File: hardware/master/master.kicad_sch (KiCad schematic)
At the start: 0 parts

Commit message: Add master card master meter sheet
Stereo 12-segment peak meter after the master level: per-side
superdiode detectors with 1 ms attack and 1.5 s fall, one shared 1%
ladder (within 0.04 dB) and 24 LM339 comparators (decision 93).

Co-Authored-By: Claude Opus 5.5 <noreply@anthropic.com>
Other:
- added sheet Master meter (meter.kicad_sch)
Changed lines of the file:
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@@
 		)
 		(pin "MAIN_L_OUT" output
-			(at 190.5 96.52 0)
+			(at 190.5 96.52 0.0000)
 			(effects
 				(font
@@
 		)
 		(pin "MAIN_R_OUT" output
-			(at 190.5 99.06 0)
+			(at 190.5 99.06 0.0000)
 			(effects
 				(font
@@
 		)
 		(pin "RLY_N" output
-			(at 190.5 101.6 0)
+			(at 190.5 101.6 0.0000)
 			(effects
 				(font
@@
 				(path "/e58f7b8d-79d3-4449-9042-9214947ce872"
 					(page "9")
+				)
+			)
+		)
+	)
+	(sheet
+		(at 215.9 38.1)
+		(size 30.48 20.32)
+		(exclude_from_sim no)
+		(in_bom yes)
+		(on_board yes)
+		(dnp no)
+		(fields_autoplaced yes)
+		(stroke
+			(width 0.1524)
+			(type solid)
+		)
+		(fill
+			(color 0 0 0 0.0000)
+		)
+		(property "Sheetname" "Master meter"
+			(at 215.9 37.3884 0)
+			(effects
+				(font
+					(size 1.27 1.27)
+				)
+				(justify left bottom)
+			)
+		)
+		(property "Sheetfile" "meter.kicad_sch"
+			(at 215.9 59.0046 0)
+			(effects
+				(font
+					(size 1.27 1.27)
+				)
+				(justify left top)
+			)
+		)
+		(pin "MAIN_L_OUT" input
+			(at 215.9 40.64 180)
+			(effects
+				(font
+					(size 1.27 1.27)
+				)
+				(justify left)
+			)
+		)
+		(pin "MAIN_R_OUT" input
+			(at 215.9 43.18 180)
+			(effects
+				(font
+					(size 1.27 1.27)
+				)
+				(justify left)
+			)
+		)
+		(instances
+			(project "master"
+				(path "/e58f7b8d-79d3-4449-9042-9214947ce872"
+					(page "10")
 				)
 			)
@@
 	(wire (pts (xy 160.02 101.6) (xy 154.94 101.6)) (stroke (width 0) (type default)))
 	(label "MAIN_R_SUM" (at 154.94 101.6 180) (fields_autoplaced yes) (effects (font (size 1.27 1.27)) (justify right bottom)))
+	(wire (pts (xy 190.5 96.52) (xy 195.58 96.52)) (stroke (width 0) (type default)))
+	(label "MAIN_L_OUT" (at 195.58 96.52 0) (fields_autoplaced yes) (effects (font (size 1.27 1.27)) (justify left bottom)))
+	(wire (pts (xy 190.5 99.06) (xy 195.58 99.06)) (stroke (width 0) (type default)))
+	(label "MAIN_R_OUT" (at 195.58 99.06 0) (fields_autoplaced yes) (effects (font (size 1.27 1.27)) (justify left bottom)))
+	(wire (pts (xy 215.9 40.64) (xy 210.82 40.64)) (stroke (width 0) (type default)))
+	(label "MAIN_L_OUT" (at 210.82 40.64 180) (fields_autoplaced yes) (effects (font (size 1.27 1.27)) (justify right bottom)))
+	(wire (pts (xy 215.9 43.18) (xy 210.82 43.18)) (stroke (width 0) (type default)))
+	(label "MAIN_R_OUT" (at 210.82 43.18 180) (fields_autoplaced yes) (effects (font (size 1.27 1.27)) (justify right bottom)))
 	(sheet_instances
 		(path "/"

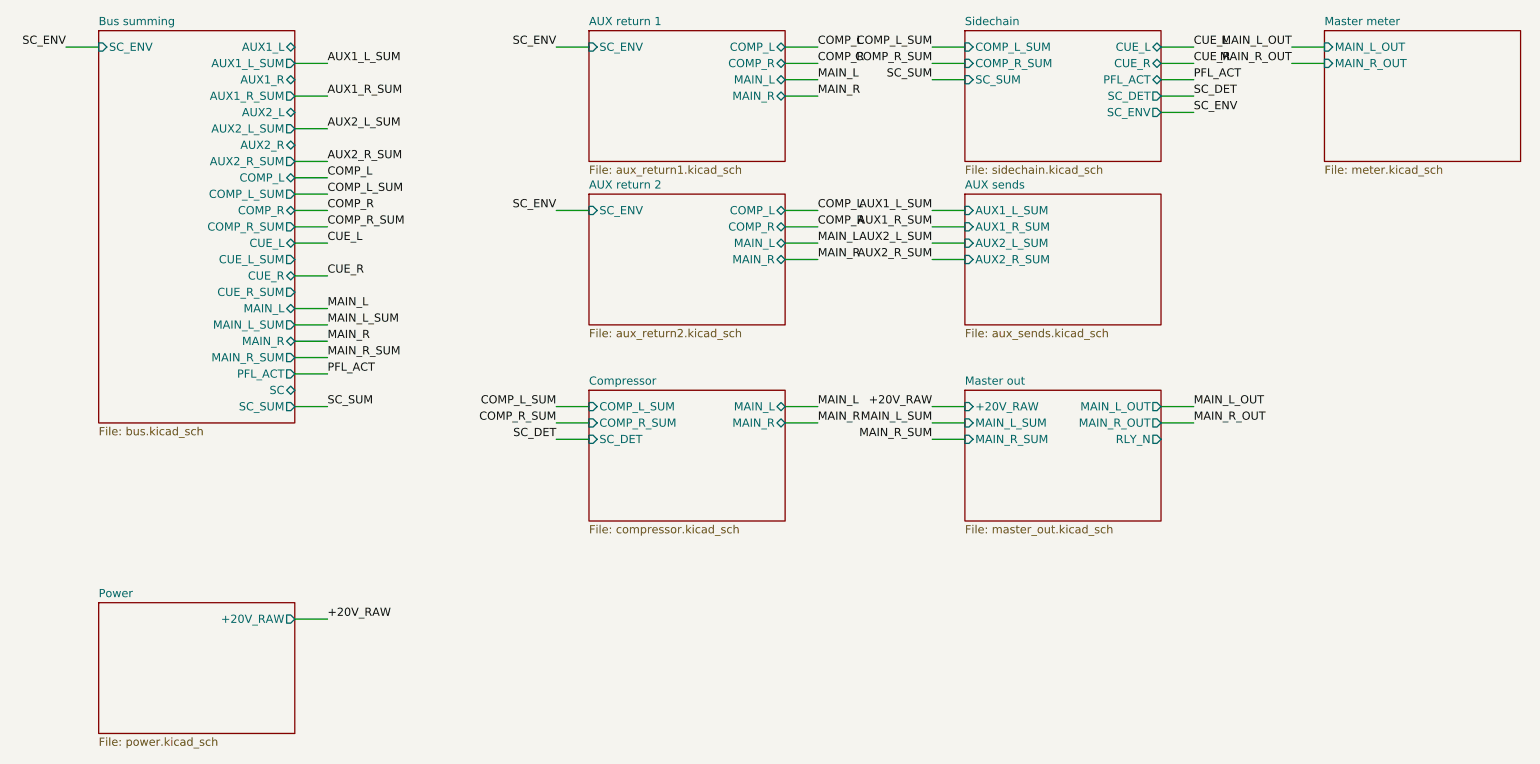
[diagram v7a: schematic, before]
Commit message: Add master card headphones sheet; master schematic complete
Main/cue source switch on PFL_ACT, dual volume pot, TPA6120A2 at
gain 2 with TI's resistor values, protection relay and PFL-active LED
(decision 94). Adds the TPA6120A2 symbol and no-connect flags for the
unused bus-node pins (root_nc.json). Master card ERC 0/0.

Co-Authored-By: Claude Opus 5.5 <noreply@anthropic.com>
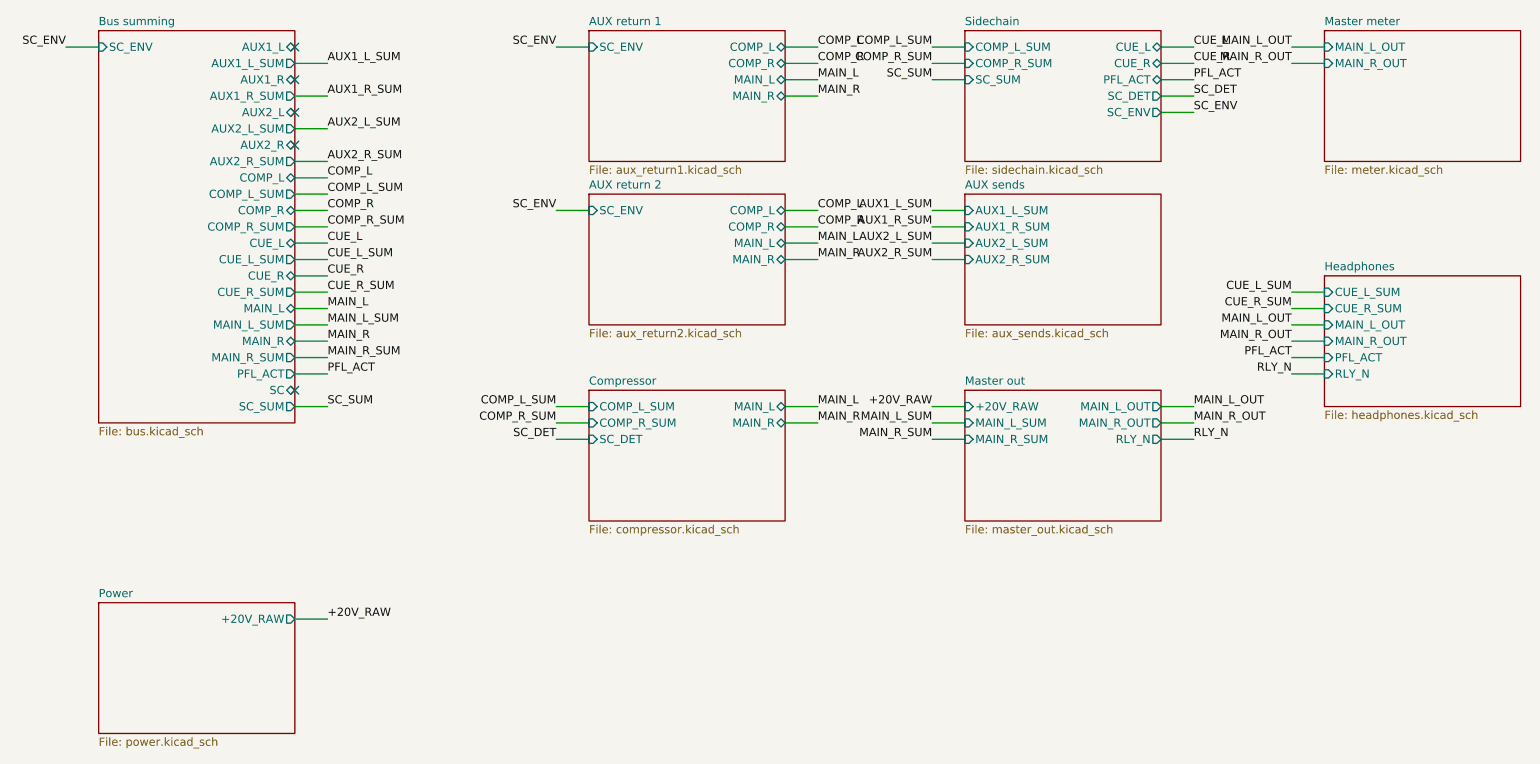
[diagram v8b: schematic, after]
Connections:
- no-connect marks 0 -> 5
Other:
- added sheet Headphones (headphones.kicad_sch)
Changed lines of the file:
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@@
+		)
+	)
+	(sheet
+		(at 215.9 76.2)
+		(size 30.48 20.32)
+		(exclude_from_sim no)
+		(in_bom yes)
+		(on_board yes)
+		(dnp no)
+		(fields_autoplaced yes)
+		(stroke
+			(width 0.1524)
+			(type solid)
+		)
+		(fill
+			(color 0 0 0 0.0000)
+		)
+		(property "Sheetname" "Headphones"
+			(at 215.9 75.4884 0)
+			(effects
+				(font
+					(size 1.27 1.27)
+				)
+				(justify left bottom)
+			)
+		)
+		(property "Sheetfile" "headphones.kicad_sch"
+			(at 215.9 97.1046 0)
+			(effects
+				(font
+					(size 1.27 1.27)
+				)
+				(justify left top)
+			)
+		)
+		(pin "CUE_L_SUM" input
+			(at 215.9 78.74 180)
+			(effects
+				(font
+					(size 1.27 1.27)
+				)
+				(justify left)
+			)
+		)
+		(pin "CUE_R_SUM" input
+			(at 215.9 81.28 180)
+			(effects
+				(font
+					(size 1.27 1.27)
+				)
+				(justify left)
+			)
+		)
+		(pin "MAIN_L_OUT" input
+			(at 215.9 83.82 180)
+			(effects
+				(font
+					(size 1.27 1.27)
+				)
+				(justify left)
+			)
+		)
+		(pin "MAIN_R_OUT" input
+			(at 215.9 86.36 180)
+			(effects
+				(font
+					(size 1.27 1.27)
+				)
+				(justify left)
+			)
+		)
+		(pin "PFL_ACT" input
+			(at 215.9 88.9 180)
+			(effects
+				(font
+					(size 1.27 1.27)
+				)
+				(justify left)
+			)
+		)
+		(pin "RLY_N" input
+			(at 215.9 91.44 180)
+			(effects
+				(font
+					(size 1.27 1.27)
+				)
+				(justify left)
+			)
+		)
+		(instances
+			(project "master"
+				(path "/e58f7b8d-79d3-4449-9042-9214947ce872"
+					(page "11")
+				)
+			)
 		)
 	)
 	(wire (pts (xy 25.4 40.64) (xy 20.32 40.64)) (stroke (width 0) (type default)))
 	(label "SC_ENV" (at 20.32 40.64 180) (fields_autoplaced yes) (effects (font (size 1.27 1.27)) (justify right bottom)))
+	(no_connect (at 55.88 40.64))
 	(wire (pts (xy 55.88 43.18) (xy 60.96 43.18)) (stroke (width 0) (type default)))
 	(label "AUX1_L_SUM" (at 60.96 43.18 0) (fields_autoplaced yes) (effects (font (size 1.27 1.27)) (justify left bottom)))
+	(no_connect (at 55.88 45.72))
 	(wire (pts (xy 55.88 48.26) (xy 60.96 48.26)) (stroke (width 0) (type default)))
 	(label "AUX1_R_SUM" (at 60.96 48.26 0) (fields_autoplaced yes) (effects (font (size 1.27 1.27)) (justify left bottom)))
+	(no_connect (at 55.88 50.8))
 	(wire (pts (xy 55.88 53.34) (xy 60.96 53.34)) (stroke (width 0) (type default)))
 	(label "AUX2_L_SUM" (at 60.96 53.34 0) (fields_autoplaced yes) (effects (font (size 1.27 1.27)) (justify left bottom)))
+	(no_connect (at 55.88 55.88))
 	(wire (pts (xy 55.88 58.42) (xy 60.96 58.42)) (stroke (width 0) (type default)))
 	(label "AUX2_R_SUM" (at 60.96 58.42 0) (fields_autoplaced yes) (effects (font (size 1.27 1.27)) (justify left bottom)))
@@
 	(wire (pts (xy 55.88 71.12) (xy 60.96 71.12)) (stroke (width 0) (type default)))
 	(label "CUE_L" (at 60.96 71.12 0) (fields_autoplaced yes) (effects (font (size 1.27 1.27)) (justify left bottom)))
+	(wire (pts (xy 55.88 73.66) (xy 60.96 73.66)) (stroke (width 0) (type default)))
+	(label "CUE_L_SUM" (at 60.96 73.66 0) (fields_autoplaced yes) (effects (font (size 1.27 1.27)) (justify left bottom)))
 	(wire (pts (xy 55.88 76.2) (xy 60.96 76.2)) (stroke (width 0) (type default)))
 	(label "CUE_R" (at 60.96 76.2 0) (fields_autoplaced yes) (effects (font (size 1.27 1.27)) (justify left bottom)))
+	(wire (pts (xy 55.88 78.74) (xy 60.96 78.74)) (stroke (width 0) (type default)))
+	(label "CUE_R_SUM" (at 60.96 78.74 0) (fields_autoplaced yes) (effects (font (size 1.27 1.27)) (justify left bottom)))
 	(wire (pts (xy 55.88 81.28) (xy 60.96 81.28)) (stroke (width 0) (type default)))
 	(label "MAIN_L" (at 60.96 81.28 0) (fields_autoplaced yes) (effects (font (size 1.27 1.27)) (justify left bottom)))
@@
 	(wire (pts (xy 55.88 91.44) (xy 60.96 91.44)) (stroke (width 0) (type default)))
 	(label "PFL_ACT" (at 60.96 91.44 0) (fields_autoplaced yes) (effects (font (size 1.27 1.27)) (justify left bottom)))
+	(no_connect (at 55.88 93.98))
 	(wire (pts (xy 55.88 96.52) (xy 60.96 96.52)) (stroke (width 0) (type default)))
 	(label "SC_SUM" (at 60.96 96.52 0) (fields_autoplaced yes) (effects (font (size 1.27 1.27)) (justify left bottom)))
@@
 	(wire (pts (xy 190.5 99.06) (xy 195.58 99.06)) (stroke (width 0) (type default)))
 	(label "MAIN_R_OUT" (at 195.58 99.06 0) (fields_autoplaced yes) (effects (font (size 1.27 1.27)) (justify left bottom)))
+	(wire (pts (xy 190.5 101.6) (xy 195.58 101.6)) (stroke (width 0) (type default)))
+	(label "RLY_N" (at 195.58 101.6 0) (fields_autoplaced yes) (effects (font (size 1.27 1.27)) (justify left bottom)))
 	(wire (pts (xy 215.9 40.64) (xy 210.82 40.64)) (stroke (width 0) (type default)))
 	(label "MAIN_L_OUT" (at 210.82 40.64 180) (fields_autoplaced yes) (effects (font (size 1.27 1.27)) (justify right bottom)))
 	(wire (pts (xy 215.9 43.18) (xy 210.82 43.18)) (stroke (width 0) (type default)))
 	(label "MAIN_R_OUT" (at 210.82 43.18 180) (fields_autoplaced yes) (effects (font (size 1.27 1.27)) (justify right bottom)))
+	(wire (pts (xy 215.9 78.74) (xy 210.82 78.74)) (stroke (width 0) (type default)))
+	(label "CUE_L_SUM" (at 210.82 78.74 180) (fields_autoplaced yes) (effects (font (size 1.27 1.27)) (justify right bottom)))
+	(wire (pts (xy 215.9 81.28) (xy 210.82 81.28)) (stroke (width 0) (type default)))
+	(label "CUE_R_SUM" (at 210.82 81.28 180) (fields_autoplaced yes) (effects (font (size 1.27 1.27)) (justify right bottom)))
+	(wire (pts (xy 215.9 83.82) (xy 210.82 83.82)) (stroke (width 0) (type default)))
+	(label "MAIN_L_OUT" (at 210.82 83.82 180) (fields_autoplaced yes) (effects (font (size 1.27 1.27)) (justify right bottom)))
+	(wire (pts (xy 215.9 86.36) (xy 210.82 86.36)) (stroke (width 0) (type default)))
+	(label "MAIN_R_OUT" (at 210.82 86.36 180) (fields_autoplaced yes) (effects (font (size 1.27 1.27)) (justify right bottom)))
+	(wire (pts (xy 215.9 88.9) (xy 210.82 88.9)) (stroke (width 0) (type default)))
+	(label "PFL_ACT" (at 210.82 88.9 180) (fields_autoplaced yes) (effects (font (size 1.27 1.27)) (justify right bottom)))
+	(wire (pts (xy 215.9 91.44) (xy 210.82 91.44)) (stroke (width 0) (type default)))
+	(label "RLY_N" (at 210.82 91.44 180) (fields_autoplaced yes) (effects (font (size 1.27 1.27)) (justify right bottom)))
 	(sheet_instances
 		(path "/"
